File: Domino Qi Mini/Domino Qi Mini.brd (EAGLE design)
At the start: 55.9 x 33 mm, 97 parts, among them J1 MH22-1, J2 MH22-1, M1 DOMINO, Q1 AP2302GN, Q2 2SC4081, SW1 IT-1210, SW2 IT-1210, SW3 IT-1210, U1 ATMEGA32U4-XUAU/MU, U2 MP2162GQH, U3 NTB0104GU12, U4 NTB0102GU, U5 MAX3375EEKA+T, U6 MP65151DJ, Y1 16MHz

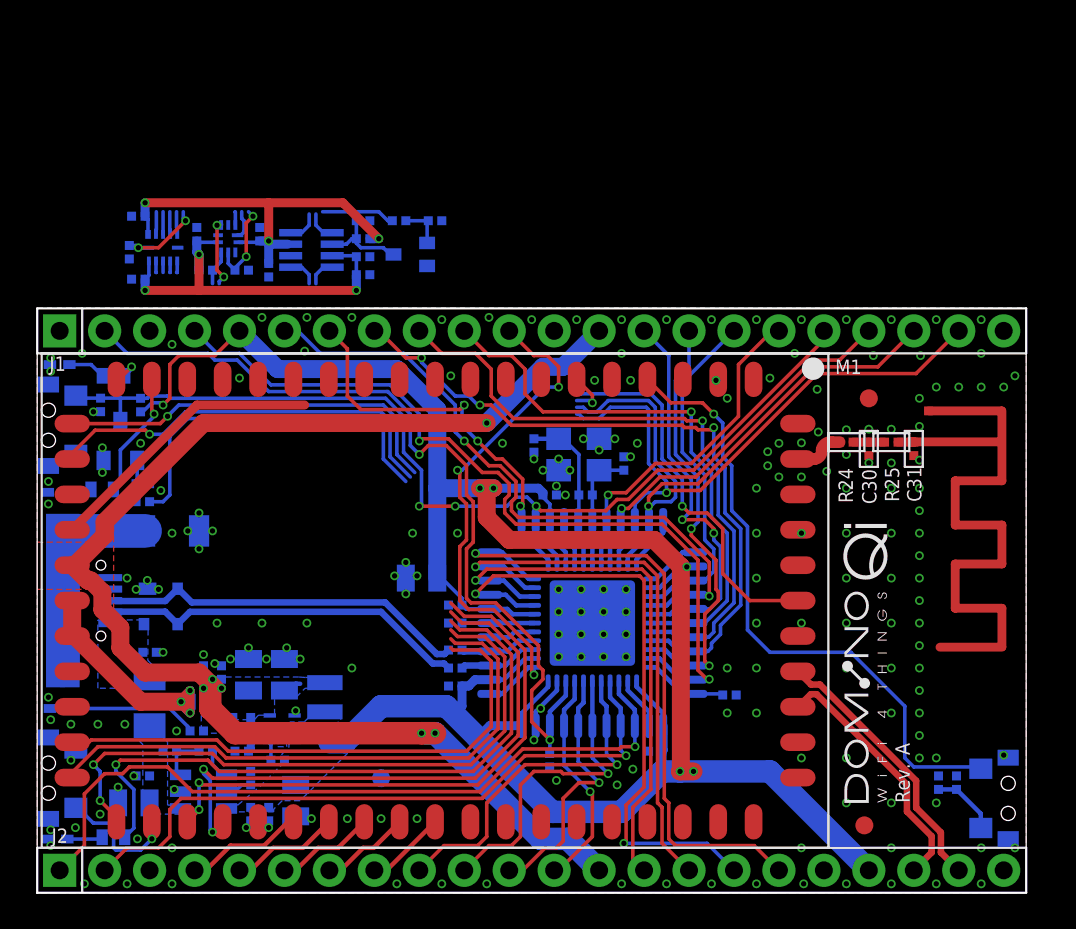
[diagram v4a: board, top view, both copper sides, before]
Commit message: Domino Qi Mini: only 20 airwires left
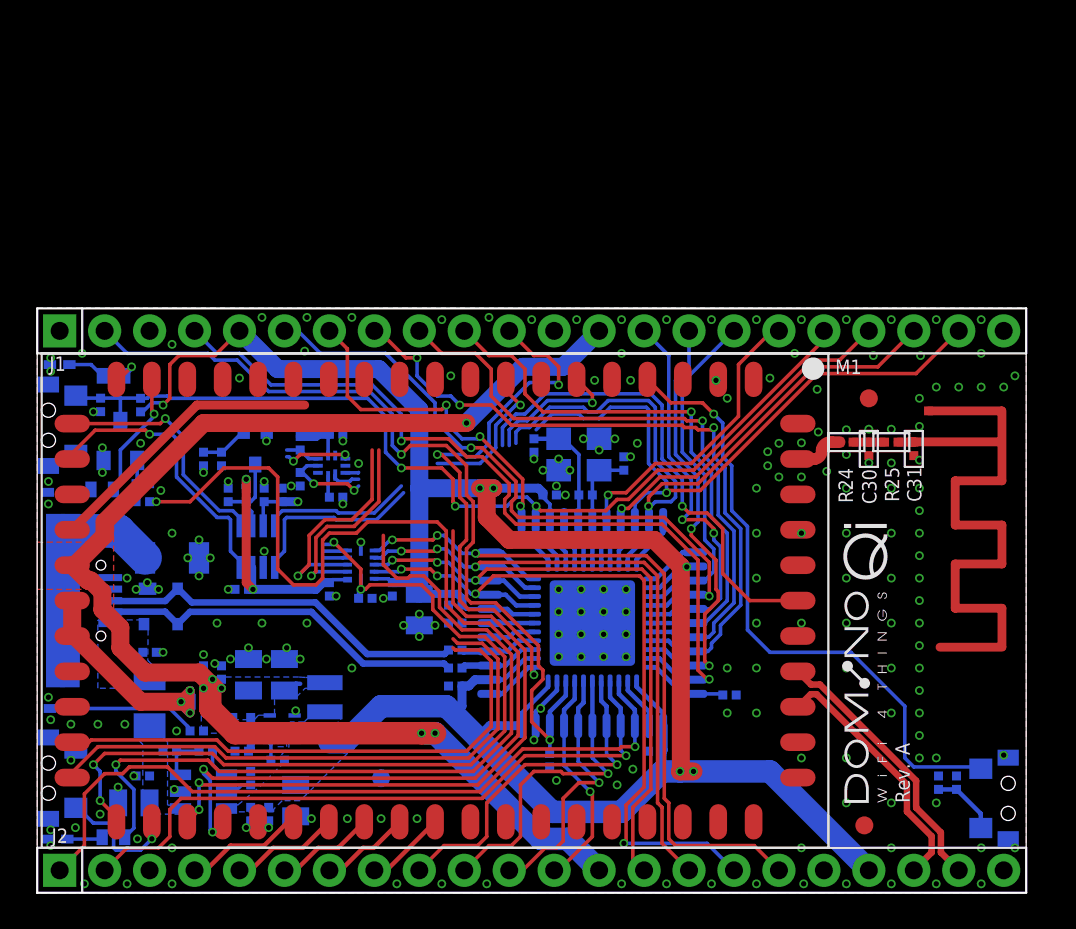
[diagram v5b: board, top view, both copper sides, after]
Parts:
- moved C26 23.7 mm to (16.5, 17.1), turned to 270 degrees
- moved R16 23.7 mm to (18.5, 16.6), turned to 0 degrees
- moved C19 22.7 mm to (20.1, 17.1), turned to 270 degrees
- moved U3 21.1 mm to (18.3, 18.5), turned to 180 degrees
- moved R13 18.8 mm to (9.40, 24.5), turned to 270 degrees
- moved C28 18.1 mm to (11.6, 17.1), turned to 0 degrees
- moved R11 17.3 mm to (10.8, 22.5), turned to 90 degrees
- moved U5 17.0 mm to (12.4, 19.6), turned to 0 degrees
- moved R15 16.8 mm to (10.4, 24.5), turned to 270 degrees
- moved R10 15.9 mm to (11.8, 22.5), turned to 90 degrees
- moved C27 15.5 mm to (16.9, 22.4), turned to 180 degrees
- moved C18 14.6 mm to (12.8, 22.5), turned to 270 degrees
- moved U4 14.1 mm to (16.6, 24.1), turned to 90 degrees
- moved Q2 14.0 mm to (12.3, 25.1), turned to 180 degrees
- moved C20 13.8 mm to (16.9, 25.9), turned to 180 degrees
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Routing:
- net +5V: track 138.9 -> 127.4 mm, vias 9 -> 7
- net LED7: track 1.28 -> 12.8 mm, vias 0 -> 1
- net TXD1: track 34.1 -> 45.6 mm
- net RXD1: track 34.6 -> 45.9 mm
- net UART_RX: track 24.3 -> 13.6 mm
- net LED8: track 1.29 -> 11.7 mm, vias 0 -> 1
- net I2S_CK: track 54.1 -> 63.9 mm, vias 2 -> 3
- net UART_TX: track 25.2 -> 16.1 mm
- net JTAG_TDI: track 1.69 -> 10.3 mm, vias 0 -> 1
- net +2V5: track 39.1 -> 31.2 mm, vias 3 -> 2
- net LED6: track 37.0 -> 44.4 mm
- net I2S_MCK: track 41.4 -> 48.1 mm
- net UART_RTS: track 22.8 -> 28.8 mm
- net MISO: track 34.8 -> 40.6 mm, vias 1 -> 3
- net SS: track 33.8 -> 39.5 mm, vias 2 -> 4
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
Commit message: Domino Qi Mini: Work in progress, only 8 airwires left
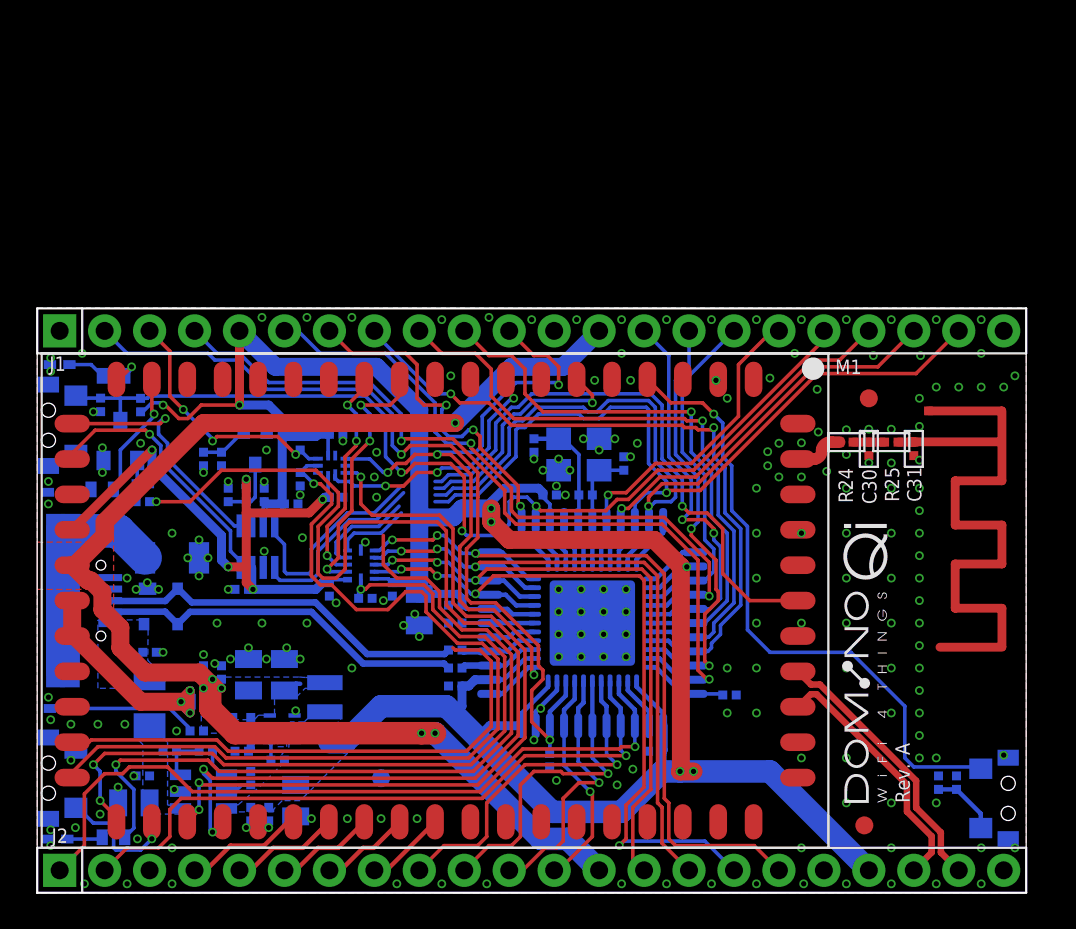
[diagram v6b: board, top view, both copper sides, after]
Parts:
- moved C21 0.72 mm to (14.4, 22.0), turned to 180 degrees
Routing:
- net I2S_MICIN: track 37.8 -> 52.2 mm, vias 2 -> 1
- net GP6: track 1.97 -> 14.5 mm, vias 0 -> 3
- net TXD1: track 45.6 -> 55.7 mm
- net JTAG_TMS: track 9.31 -> 19.4 mm
- net +5V: track 127.4 -> 136.9 mm
- net RXD1: track 45.9 -> 54.5 mm
- net UART_RTS: track 28.8 -> 36.7 mm
- net I2S_WS: track 37.0 -> 44.7 mm, vias 2 -> 3
- net +2V5: track 31.2 -> 36.0 mm, vias 2 -> 5
- net JTAG_TDI: track 10.3 -> 14.7 mm, vias 1 -> 3
- net !RESET: track 54.1 -> 58.0 mm
- net I2S_MCK: track 48.1 -> 44.3 mm, vias 4 -> 3
- net LED8: track 11.7 -> 15.0 mm, vias 1 -> 3
- net HANDSHAKE: track 34.3 -> 37.1 mm, vias 5 -> 4
- net UART_TX: track 16.1 -> 15.0 mm
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
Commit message: Domino Qi Mini: only 1 airwire left!
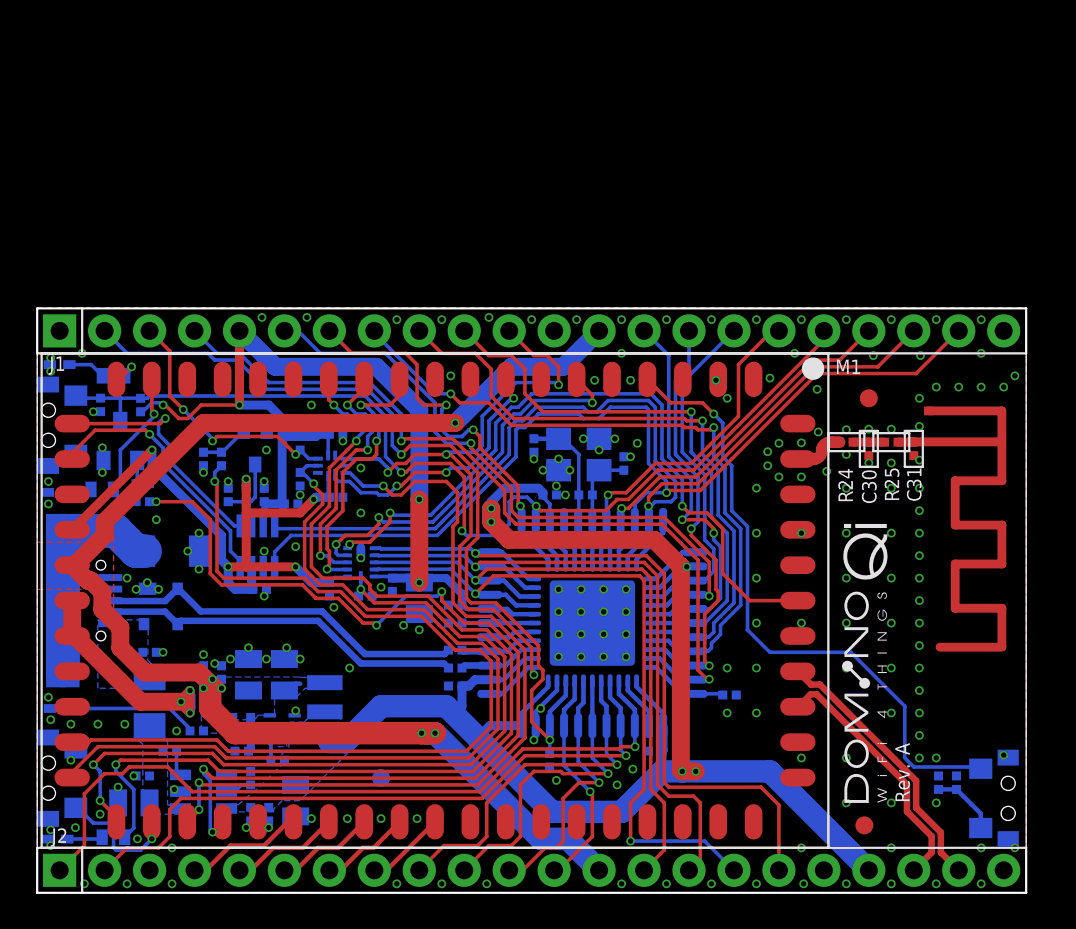
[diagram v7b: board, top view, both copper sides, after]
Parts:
- removed R28: 0R, Domino:R0402
- moved C28 1.02 mm to (12.6, 17.1), turned to 180 degrees
- moved C7 0.64 mm to (21.6, 16.6)
- moved C1 0.38 mm to (7.62, 19.3)
- moved C19 0.25 mm to (20.1, 17.4)
- moved R16 0.13 mm to (18.5, 16.8)
- moved U3 0.13 mm to (18.3, 18.7)
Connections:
- removed net !FLAG: R28.1, U6.4
- net EN_USB: no longer R28.2
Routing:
- net SPDIF_OUT: track 30.7 -> 52.0 mm, vias 0 -> 1
- net LED6: track 44.3 -> 59.5 mm, vias 1 -> 3
- net I2S_CK: track 64.9 -> 56.3 mm, vias 3 -> 5
- net +5V: track 136.9 -> 132.6 mm, vias 7 -> 9
- net JTAG_TMS: track 19.4 -> 22.1 mm, vias 1 -> 3
- net UART_RTS: track 36.7 -> 39.4 mm, vias 1 -> 3
- net TXD1: track 55.7 -> 53.3 mm
- net LED7: track 12.6 -> 14.5 mm
- net !FLAG: track 1.79 -> 0.00 mm
- net I2S_MICIN: track 52.2 -> 50.5 mm
- net +2V5: track 36.0 -> 37.5 mm
- net SS: track 40.1 -> 38.8 mm, vias 4 -> 2
- net I2S_WS: track 44.7 -> 45.9 mm
- net EN_USB: track 2.70 -> 1.43 mm
- net LED8: track 15.0 -> 16.2 mm
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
